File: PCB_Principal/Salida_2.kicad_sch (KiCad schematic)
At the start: 41 parts, among them Q81 BC807, Q82 BC559C, Q83 BC549C, Q84 BC549C, Q85 BC559C, Q86 2SD882, Q87 2SB772, U81 LM318

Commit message: Iniciando PCB...
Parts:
- renumbered C81 to C251, C82 to C252, C83 to C253, C84 to C254, C85 to C255, C86 to C256, C87 to C257, D82 to D251, D83 to D252, D84 to D253, D85 to D254, F81 to F251, Q81 to Q251, Q82 to Q252, Q83 to Q253, Q84 to Q254, Q85 to Q255, Q86 to Q256, Q87 to Q257, R81 to R251, R83 to R252, R84 to R253, R82 to R254, R85 to R255, R86 to R256, R87 to R257, R88 to R258, R89 to R259, R90 to R260, R91 to R261, R92 to R262, R93 to R263, R94 to R264, R95 to R265, R96 to R266, R97 to R267, R98 to R268, R99 to R269, R100 to R270, RV81 to RV251, U81 to U251

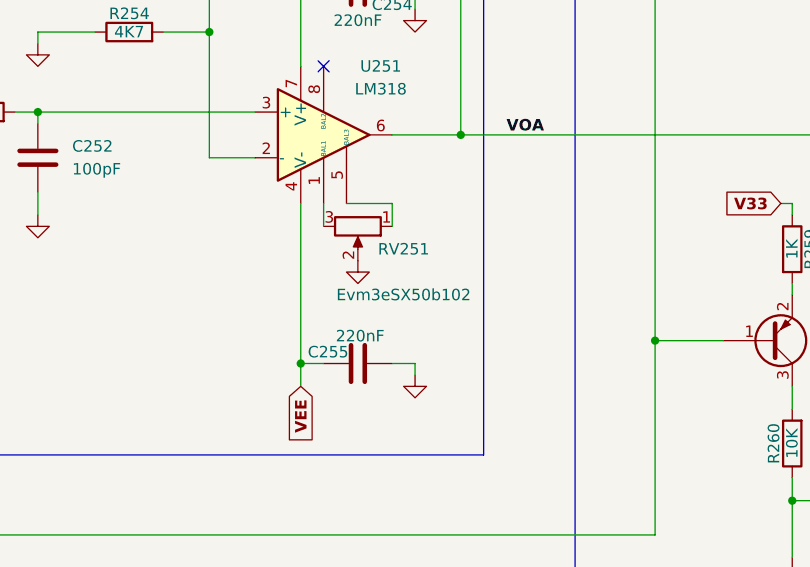
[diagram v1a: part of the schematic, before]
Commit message: Placa con conector J8.
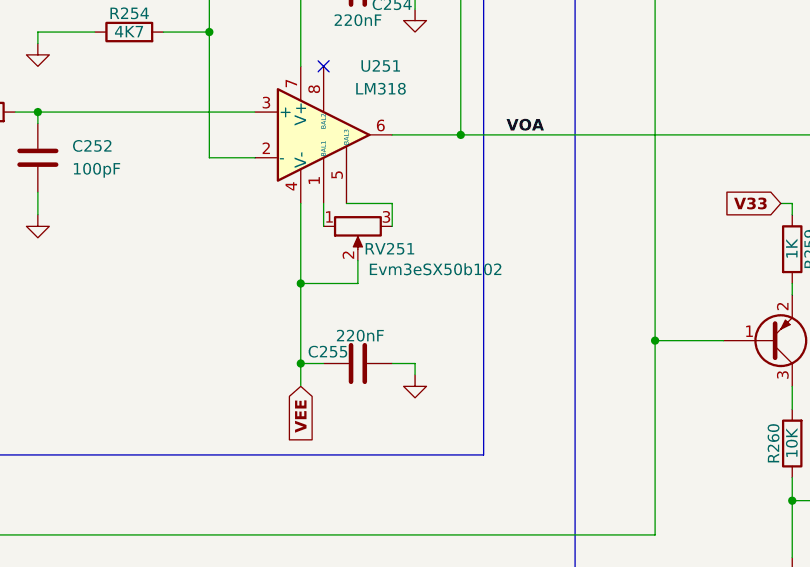
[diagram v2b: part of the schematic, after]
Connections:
- net GND: no longer RV251.2
- net VEE: now also RV251.2
- net at RV251.1: now also U251.1 (BAL1); no longer U251.5 (BAL3)
- net at RV251.3: now also U251.5 (BAL3); no longer U251.1 (BAL1)
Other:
- moved on the sheet: RV251
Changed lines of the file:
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@@
+	)
+	(junction
+		(at 74.93 99.06)
+		(diameter 0)
+		(color 0 0 0 0)
 	)
 	(junction
@@
 	(wire
 		(pts
+			(xy 74.93 99.06) (xy 81.28 99.06)
+		)
+		(stroke
+			(width 0)
+			(type default)
+		)
+	)
+	(wire
+		(pts
 			(xy 74.93 66.04) (xy 77.47 66.04)
 		)
@@
 	(wire
 		(pts
+			(xy 74.93 99.06) (xy 74.93 107.95)
+		)
+		(stroke
+			(width 0)
+			(type default)
+		)
+	)
+	(wire
+		(pts
 			(xy 195.58 72.39) (xy 195.58 73.66)
 		)
@@
 	(wire
 		(pts
-			(xy 74.93 90.17) (xy 74.93 107.95)
+			(xy 81.28 96.52) (xy 81.28 99.06)
+		)
+		(stroke
+			(width 0)
+			(type default)
+		)
+	)
+	(wire
+		(pts
+			(xy 74.93 90.17) (xy 74.93 99.06)
 		)
 		(stroke
@@
 	)
 	(symbol
-		(lib_id "power:GND")
-		(at 81.28 96.52 0)
-		(unit 1)
-		(exclude_from_sim no)
-		(in_bom yes)
-		(on_board yes)
-		(dnp no)
-		(fields_autoplaced yes)
-		(property "Reference" "#PWR0254"
-			(at 81.28 102.87 0)
-			(effects
-				(font
-					(size 1.27 1.27)
-				)
-				(hide yes)
-			)
-		)
-		(property "Value" "GND"
-			(at 81.28 101.6 0)
-			(effects
-				(font
-					(size 1.27 1.27)
-				)
-				(hide yes)
-			)
-		)
-		(property "Footprint" ""
-			(at 81.28 96.52 0)
-			(effects
-				(font
-					(size 1.27 1.27)
-				)
-				(hide yes)
-			)
-		)
-		(property "Datasheet" ""
-			(at 81.28 96.52 0)
-			(effects
-				(font
-					(size 1.27 1.27)
-				)
-				(hide yes)
-			)
-		)
-		(property "Description" "Power symbol creates a global label with name \"GND\" , ground"
-			(at 81.28 96.52 0)
-			(effects
-				(font
-					(size 1.27 1.27)
-				)
-				(hide yes)
-			)
-		)
-		(pin "1"
-		)
-		(instances
-			(project "ISPEL-CAD_v1"
-				(path "/f66f0001-c0b9-4d2c-a26f-f2bac9dfd594/1daac50b-8155-4482-83b0-91b256970459"
-					(reference "#PWR0254")
-					(unit 1)
-				)
-			)
-		)
-	)
-	(symbol
 		(lib_id "Device:C")
 		(at 45.72 58.42 0)
@@
 	(symbol
 		(lib_id "Device:R_Potentiometer")
-		(at 81.28 92.71 270)
+		(at 81.28 92.71 90)
+		(mirror x)
 		(unit 1)
 		(exclude_from_sim no)
@@
 		(dnp no)
 		(property "Reference" "RV251"
-			(at 86.36 95.25 90)
+			(at 84.836 95.25 90)
 			(effects
 				(font
@@
 		)
 		(property "Value" "Evm3eSX50b102"
-			(at 86.36 100.33 90)
-			(effects
-				(font
+			(at 89.916 97.536 90)
+			(effects
+				(font

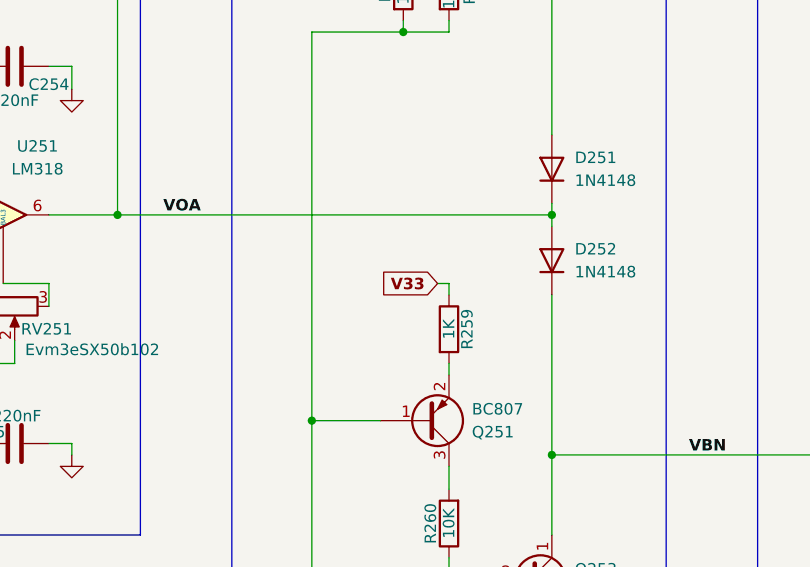
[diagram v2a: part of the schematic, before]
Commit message: Placa PCB con ERC. Falta huella de portafusibles.
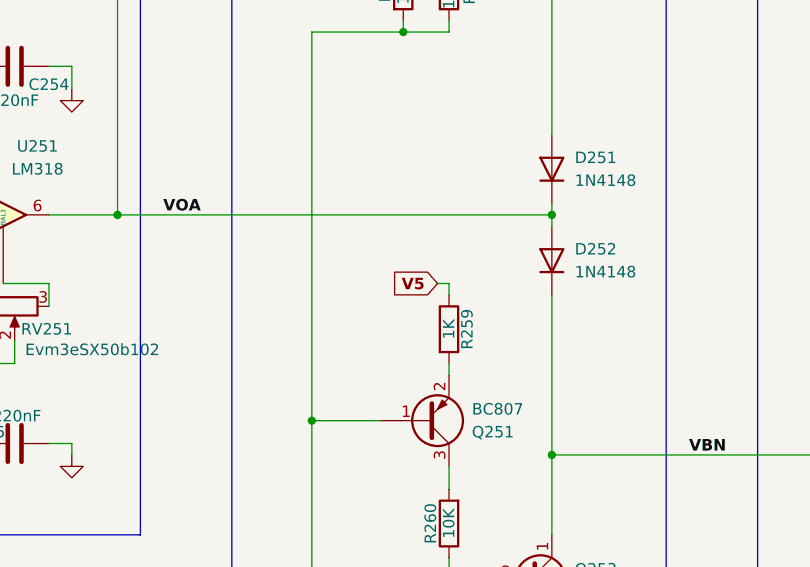
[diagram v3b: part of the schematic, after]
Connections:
- net V33 renamed V5
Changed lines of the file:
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@@
 		)
 	)
-	(global_label "V33"
+	(global_label "V5"
 		(shape input)
 		(at 128.27 90.17 180)
@@
 		)
 		(property "Intersheetrefs" "${INTERSHEET_REFS}"
-			(at 121.3012 90.17 0)
+			(at 122.5107 90.17 0)
 			(effects
 				(font

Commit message: PCB con huella de portafusibles 1808.
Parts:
- F251: footprint Fuse:Fuse_1812_4532Metric_Pad1.30x3.40mm_HandSolder -> Libreria_ISPEL:Fuseholder_1808_handsoldering
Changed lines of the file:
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@@
 			)
 		)
-		(property "Footprint" "Fuse:Fuse_1812_4532Metric_Pad1.30x3.40mm_HandSolder"
+		(property "Footprint" "Libreria_ISPEL:Fuseholder_1808_handsoldering"
 			(at 237.49 84.328 90)
 			(effects

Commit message: Corrigiendo PCB con comentarios AS.
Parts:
- R268, R269: footprint Resistor_THT:R_Axial_DIN0414_L11.9mm_D4.5mm_P5.08mm_Vertical -> Resistor_THT:R_Axial_DIN0414_L11.9mm_D4.5mm_P15.24mm_Horizontal
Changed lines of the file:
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@@
 			)
 		)
-		(property "Footprint" "Resistor_THT:R_Axial_DIN0414_L11.9mm_D4.5mm_P5.08mm_Vertical"
+		(property "Footprint" "Resistor_THT:R_Axial_DIN0414_L11.9mm_D4.5mm_P15.24mm_Horizontal"
 			(at 237.49 72.898 90)
 			(effects
@@
 			)
 		)
-		(property "Footprint" "Resistor_THT:R_Axial_DIN0414_L11.9mm_D4.5mm_P5.08mm_Vertical"
+		(property "Footprint" "Resistor_THT:R_Axial_DIN0414_L11.9mm_D4.5mm_P15.24mm_Horizontal"
 			(at 237.49 69.088 90)
 			(effects

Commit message: Revisión 1. Con prototipo ISPEL Beta 2024 en fase de prueba.
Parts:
- R266, R267: value 1M -> CAL
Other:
- title: Salida 2 (ISPEL Beta 2024) -> Salida 2 (ISPEL Beta)
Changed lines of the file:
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@@
 	(paper "A4")
 	(title_block
-		(title "Salida 2 (ISPEL Beta 2024)")
-		(date "2024-10-29")
-		(rev "2 (GC)")
+		(title "Salida 2 (ISPEL Beta)")
+		(date "2025-04-04")
+		(rev "1")
 	)
 	(junction
@@
 			)
 		)
-		(property "Value" "1M"
+		(property "Value" "CAL"
 			(at 204.47 89.154 90)
 			(effects
@@
 			)
 		)
-		(property "Value" "1M"
+		(property "Value" "CAL"
 			(at 204.47 78.74 90)
 			(effects
